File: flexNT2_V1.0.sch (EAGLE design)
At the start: 6 parts, among them U1 NTAG-I2C+

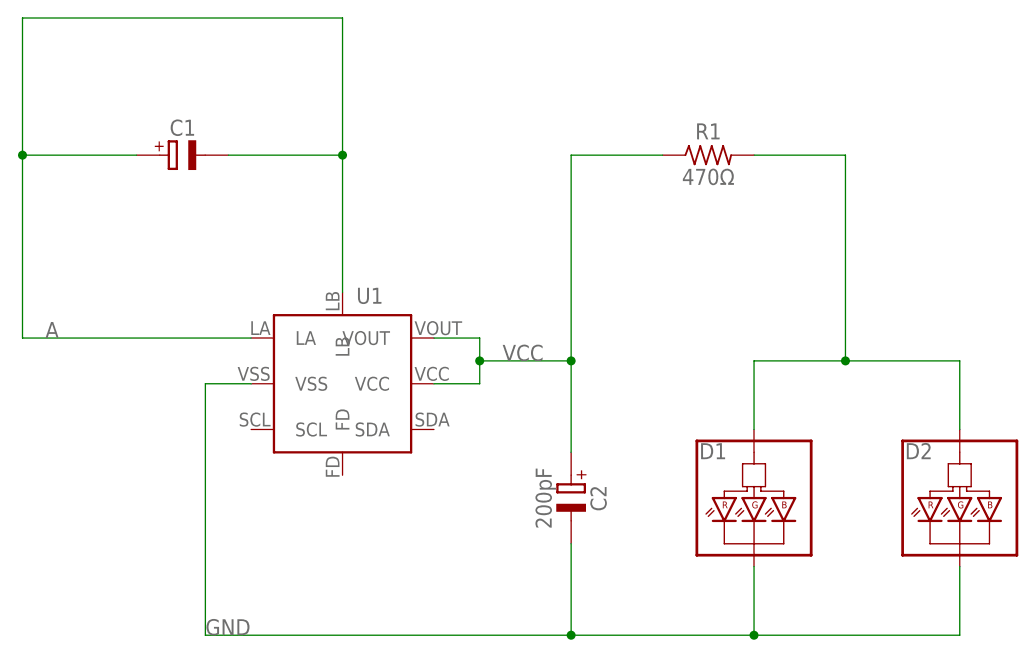
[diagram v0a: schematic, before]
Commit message: Removed power to the i2c bus of NTAG chip as not in use.
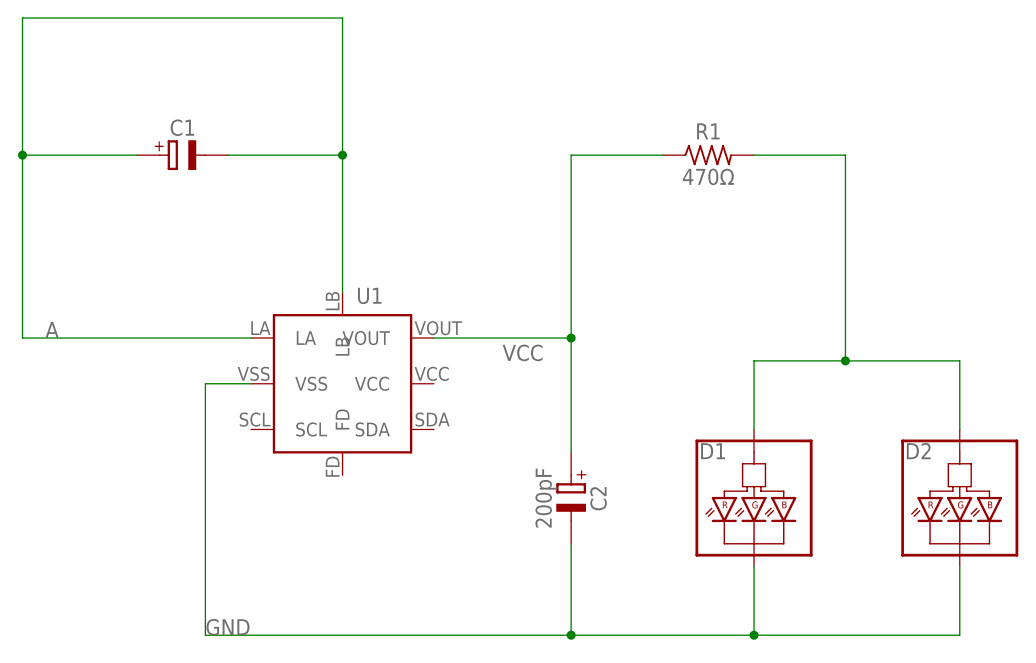
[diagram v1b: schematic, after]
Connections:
- net VCC: no longer U1.VCC
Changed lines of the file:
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@@
 <segment>
 <pinref part="U1" gate="G$1" pin="VOUT"/>
-<wire x1="66.04" y1="127" x2="71.12" y2="127" width="0.1524" layer="91"/>
-<wire x1="71.12" y1="127" x2="71.12" y2="124.46" width="0.1524" layer="91"/>
-<pinref part="U1" gate="G$1" pin="VCC"/>
-<wire x1="71.12" y1="124.46" x2="71.12" y2="121.92" width="0.1524" layer="91"/>
-<wire x1="71.12" y1="121.92" x2="66.04" y2="121.92" width="0.1524" layer="91"/>
-<wire x1="71.12" y1="124.46" x2="81.28" y2="124.46" width="0.1524" layer="91"/>
-<junction x="71.12" y="124.46"/>
-<wire x1="81.28" y1="124.46" x2="81.28" y2="147.32" width="0.1524" layer="91"/>
+<wire x1="66.04" y1="127" x2="81.28" y2="127" width="0.1524" layer="91"/>
+<wire x1="81.28" y1="127" x2="81.28" y2="147.32" width="0.1524" layer="91"/>
 <label x="73.66" y="124.46" size="1.778" layer="95"/>
 <pinref part="R1" gate="G$1" pin="1"/>
 <wire x1="81.28" y1="147.32" x2="91.44" y2="147.32" width="0.1524" layer="91"/>
 <pinref part="C2" gate="G$1" pin="+"/>
-<wire x1="81.28" y1="124.46" x2="81.28" y2="114.3" width="0.1524" layer="91"/>
-<junction x="81.28" y="124.46"/>
+<wire x1="81.28" y1="127" x2="81.28" y2="114.3" width="0.1524" layer="91"/>
+<junction x="81.28" y="127"/>
 </segment>
 </net>

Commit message: Fixed lib linking and a few other small fixes
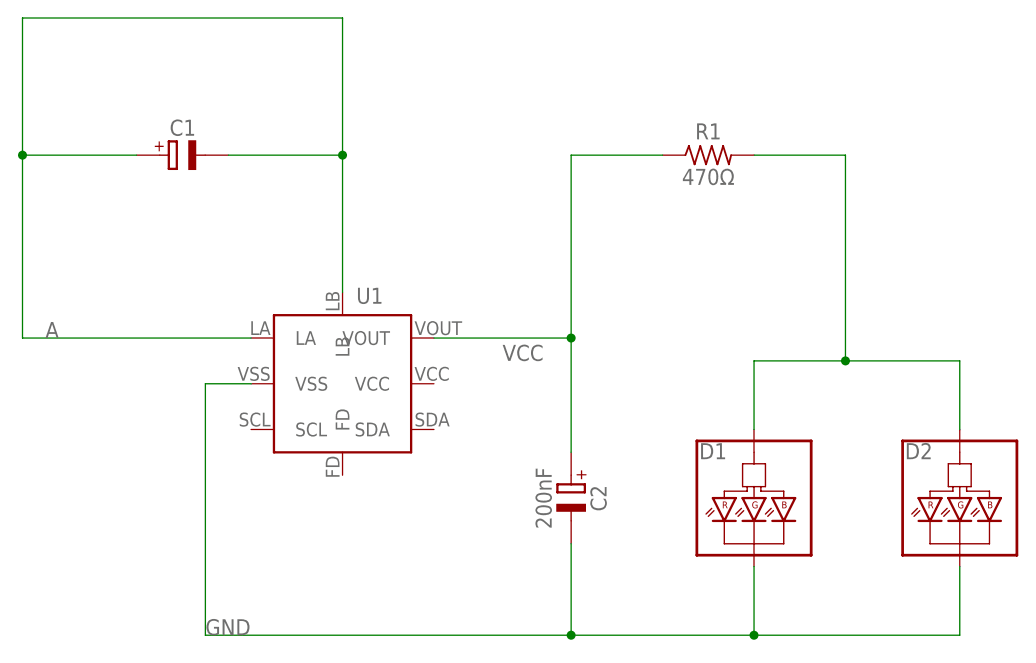
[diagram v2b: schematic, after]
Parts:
- C1: device Samuel_Collection:C_POL_0603_FLEX -> flexNT2_V1.0:C_POL_0603_FLEX
- C2: value 200pF -> 200nF; device Samuel_Collection:C_POL_0603_FLEX -> flexNT2_V1.0:C_POL_0603_FLEX
- D1, D2: device Samuel_Collection:CZINELIGHT_0807RGBFF -> flexNT2_V1.0:CZINELIGHT_0807RGBFF
- R1: device Samuel_Collection:R_0603_FLEX -> flexNT2_V1.0:R_0603_FLEX
- U1: device Samuel_Collection:NTAG-I2C+ -> flexNT2_V1.0:NTAG-I2C+
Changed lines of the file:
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@@
 </classes>
 <parts>
-<part name="FRAME1" library="frames" library_urn="urn:adsk.eagle:library:229" deviceset="A4L-LOC" device=""/>
-<part name="U1" library="Samuel_Collection" deviceset="NTAG-I2C+" device=""/>
-<part name="C1" library="Samuel_Collection" deviceset="C_POL" device="_0603_FLEX"/>
-<part name="C2" library="Samuel_Collection" deviceset="C_POL" device="_0603_FLEX" value="200pF"/>
-<part name="R1" library="Samuel_Collection" deviceset="R" device="_0603_FLEX" value="470Ω"/>
-<part name="D1" library="Samuel_Collection" deviceset="CZINELIGHT" device="_0807RGBFF"/>
-<part name="D2" library="Samuel_Collection" deviceset="CZINELIGHT" device="_0807RGBFF"/>
+<part name="FRAME1" library="flexNT2_V1.0" deviceset="A4L-LOC" device=""/>
+<part name="U1" library="flexNT2_V1.0" deviceset="NTAG-I2C+" device=""/>
+<part name="C1" library="flexNT2_V1.0" deviceset="C_POL" device="_0603_FLEX"/>
+<part name="C2" library="flexNT2_V1.0" deviceset="C_POL" device="_0603_FLEX" value="200nF"/>
+<part name="R1" library="flexNT2_V1.0" deviceset="R" device="_0603_FLEX" value="470Ω"/>
+<part name="D1" library="flexNT2_V1.0" deviceset="CZINELIGHT" device="_0807RGBFF"/>
+<part name="D2" library="flexNT2_V1.0" deviceset="CZINELIGHT" device="_0807RGBFF"/>
 </parts>
 <sheets>
@@
 </schematic>
 </drawing>
-<compatibility>
-<note version="8.2" severity="warning">
-Since Version 8.2, EAGLE supports online libraries. The ids
-of those online libraries will not be understood (or retained)
-with this version.
-</note>
-<note version="8.3" severity="warning">
-Since Version 8.3, EAGLE supports URNs for individual library
-assets (packages, symbols, and devices). The URNs of those assets
-will not be understood (or retained) with this version.
-</note>
-</compatibility>
 </eagle>
